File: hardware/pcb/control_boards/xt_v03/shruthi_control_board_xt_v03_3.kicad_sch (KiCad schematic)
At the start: 50 parts, among them IC2 74HC165N, IC3 74HC165N, IC8 74595N, IC9 74HC165N, SW1 Encoder

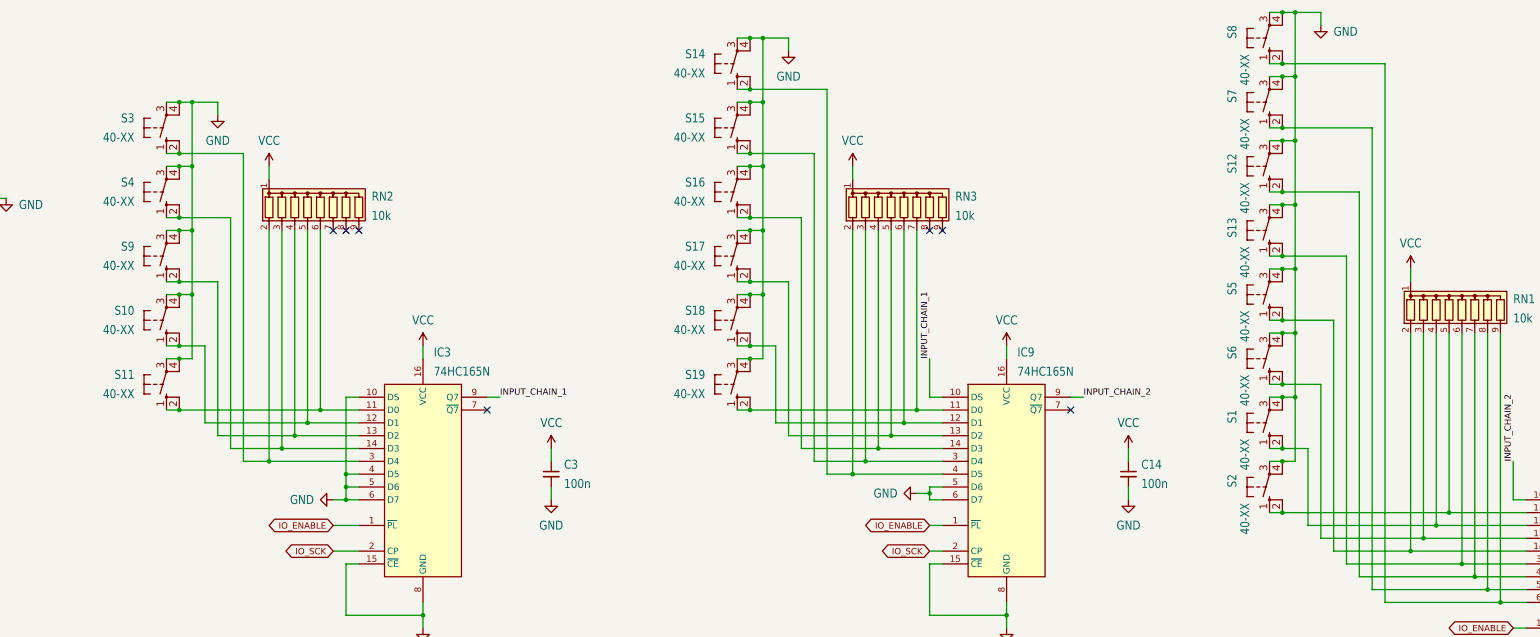
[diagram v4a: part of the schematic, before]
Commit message: update switches to use kicad symbols
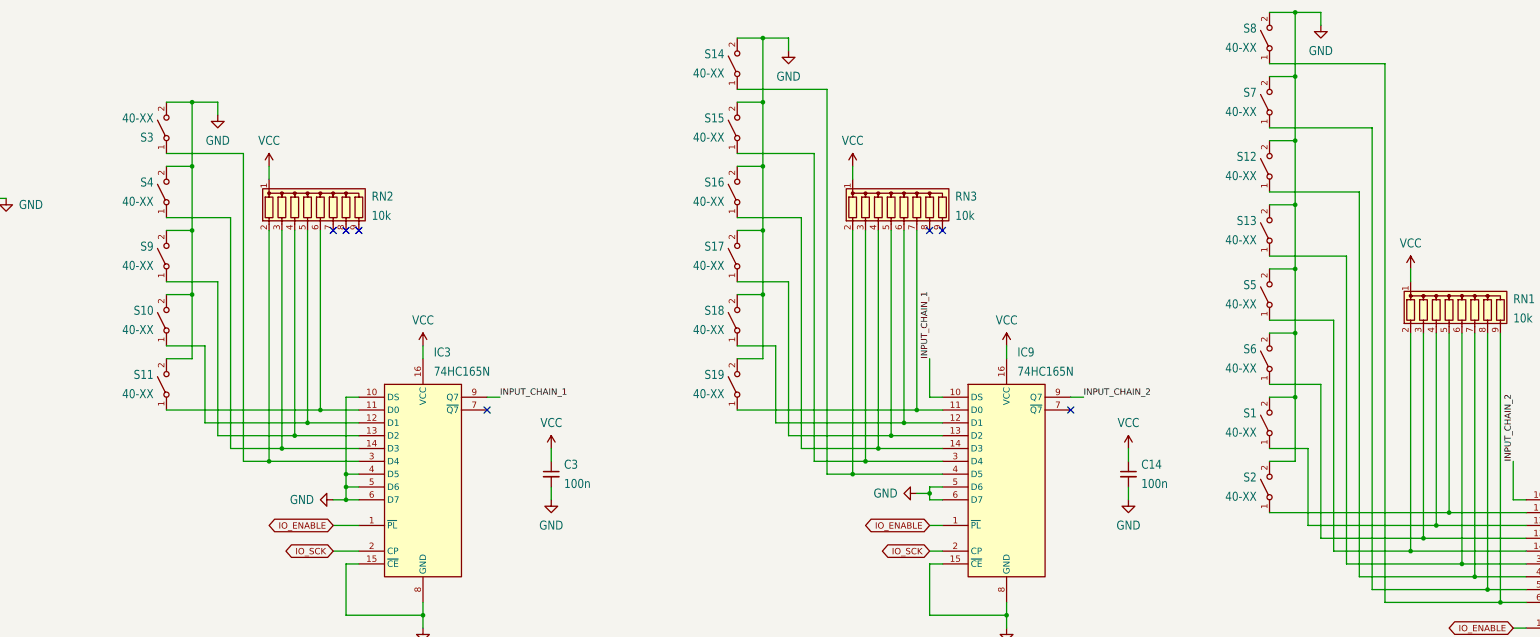
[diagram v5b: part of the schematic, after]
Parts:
- S1, S10, S11, S12, S13, S14, S15, S16, S17, S18, S19, S2, S3, S4, S5, S6, S7, S8, S9: symbol shruthi_control_board_xt_v03-eagle-import:40-XX -> Switch:SW_SPST
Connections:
- net GND: now also S1.2 (B), S10.2 (B), S11.2 (B), S12.2 (B), S13.2 (B), S14.2 (B), S15.2 (B), S16.2 (B), S17.2 (B), S18.2 (B), S19.2 (B), S2.2 (B), S3.2 (B), S4.2 (B), S5.2 (B), S6.2 (B), S7.2 (B), S8.2 (B), S9.2 (B); no longer S1.3 (P), S1.4 (P1), S10.3 (P), S10.4 (P1), S11.3 (P), S11.4 (P1), S12.3 (P), S12.4 (P1), S13.3 (P), S13.4 (P1), S14.3 (P), S14.4 (P1), S15.3 (P), S15.4 (P1), S16.3 (P), S16.4 (P1), S17.3 (P), S17.4 (P1), S18.3 (P), S18.4 (P1), S19.3 (P), S19.4 (P1), S2.3 (P), S2.4 (P1), S3.3 (P), S3.4 (P1), S4.3 (P), S4.4 (P1), S5.3 (P), S5.4 (P1), S6.3 (P), S6.4 (P1), S7.3 (P), S7.4 (P1), S8.3 (P), S8.4 (P1), S9.3 (P), S9.4 (P1)
- net at IC9.12 (D1), RN3.6 (R5), S18.1 (A): no longer S18.2 (S1)
- net at IC3.12 (D1), RN2.5 (R4), S10.1 (A): no longer S10.2 (S1)
- net at IC9.13 (D2), RN3.5 (R4), S17.1 (A): no longer S17.2 (S1)
- net at IC3.11 (D0), RN2.6 (R5), S11.1 (A): no longer S11.2 (S1)
- net at IC3.13 (D2), RN2.4 (R3), S9.1 (A): no longer S9.2 (S1)
- net at IC3.14 (D3), RN2.3 (R2), S4.1 (A): no longer S4.2 (S1)
- net at IC3.3 (D4), RN2.2 (R1), S3.1 (A): no longer S3.2 (S1)
- net at IC9.11 (D0), RN3.7 (R6), S19.1 (A): no longer S19.2 (S1)
- net at IC2.12 (D1), RN1.4 (R3), S1.1 (A): no longer S1.2 (S1)
- net at IC9.4 (D5), RN3.2 (R1), S14.1 (A): no longer S14.2 (S1)
- net at IC2.11 (D0), RN1.5 (R4), S2.1 (A): no longer S2.2 (S1)
- net at IC9.3 (D4), RN3.3 (R2), S15.1 (A): no longer S15.2 (S1)
- net at IC9.14 (D3), RN3.4 (R3), S16.1 (A): no longer S16.2 (S1)
- net at IC2.6 (D7), RN1.9 (R8), S8.1 (A): no longer S8.2 (S1)
- net at IC2.13 (D2), RN1.3 (R2), S6.1 (A): no longer S6.2 (S1)
- net at IC2.14 (D3), RN1.2 (R1), S5.1 (A): no longer S5.2 (S1)
- net at IC2.3 (D4), RN1.6 (R5), S13.1 (A): no longer S13.2 (S1)
- net at IC2.4 (D5), RN1.7 (R6), S12.1 (A): no longer S12.2 (S1)
- net at IC2.5 (D6), RN1.8 (R7), S7.1 (A): no longer S7.2 (S1)

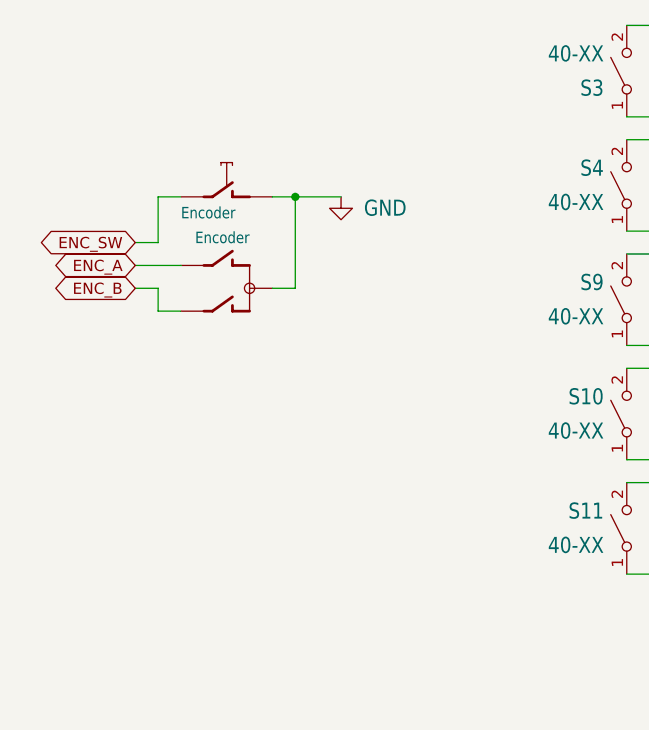
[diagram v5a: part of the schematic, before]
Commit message: update switches to use kicad symbols
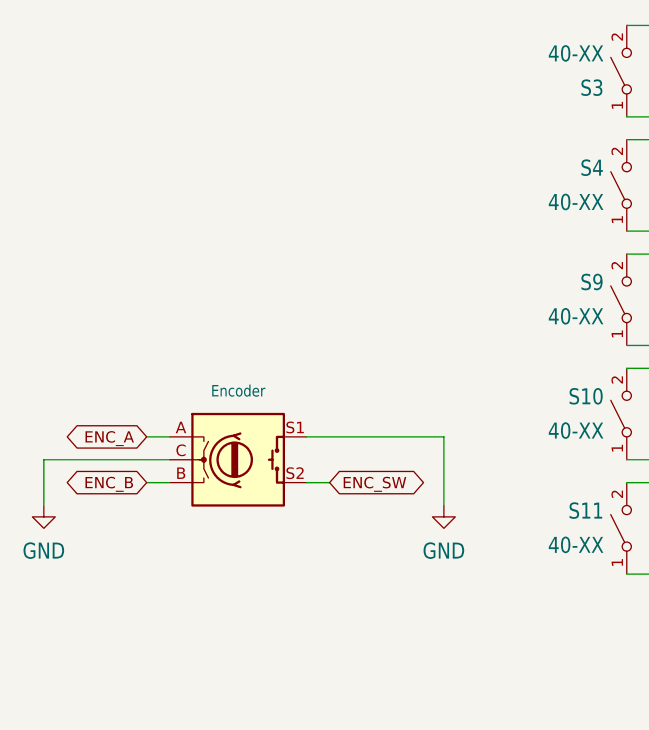
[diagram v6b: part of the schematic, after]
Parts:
- removed unit 2 of SW1
- SW1: symbol shruthi_control_board_xt_v03-eagle-import:EC12E_SW -> Device:RotaryEncoder_Switch
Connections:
- net ENC_A: now also SW1.A; no longer SW1.B
- net ENC_B: now also SW1.B; no longer SW1.A
- net ENC_SW: now also SW1.S2
- net GND: now also SW1.S1

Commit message: update 74HC165 footprints
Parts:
- IC2, IC3, IC9: footprint shruthi_control_board_xt_v03:DIL16 -> Package_DIP:DIP-16_W7.62mm_Socket_LongPads
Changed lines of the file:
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@@
 			)
 		)
-		(property "Footprint" "shruthi_control_board_xt_v03:DIL16"
+		(property "Footprint" "Package_DIP:DIP-16_W7.62mm_Socket_LongPads"
 			(at 139.7 127 0)
 			(effects
@@
 			)
 		)
-		(property "Footprint" "shruthi_control_board_xt_v03:DIL16"
+		(property "Footprint" "Package_DIP:DIP-16_W7.62mm_Socket_LongPads"
 			(at 255.27 127 0)
 			(effects
@@
 			)
 		)
-		(property "Footprint" "shruthi_control_board_xt_v03:DIL16"
+		(property "Footprint" "Package_DIP:DIP-16_W7.62mm_Socket_LongPads"
 			(at 370.84 147.32 0)
 			(effects

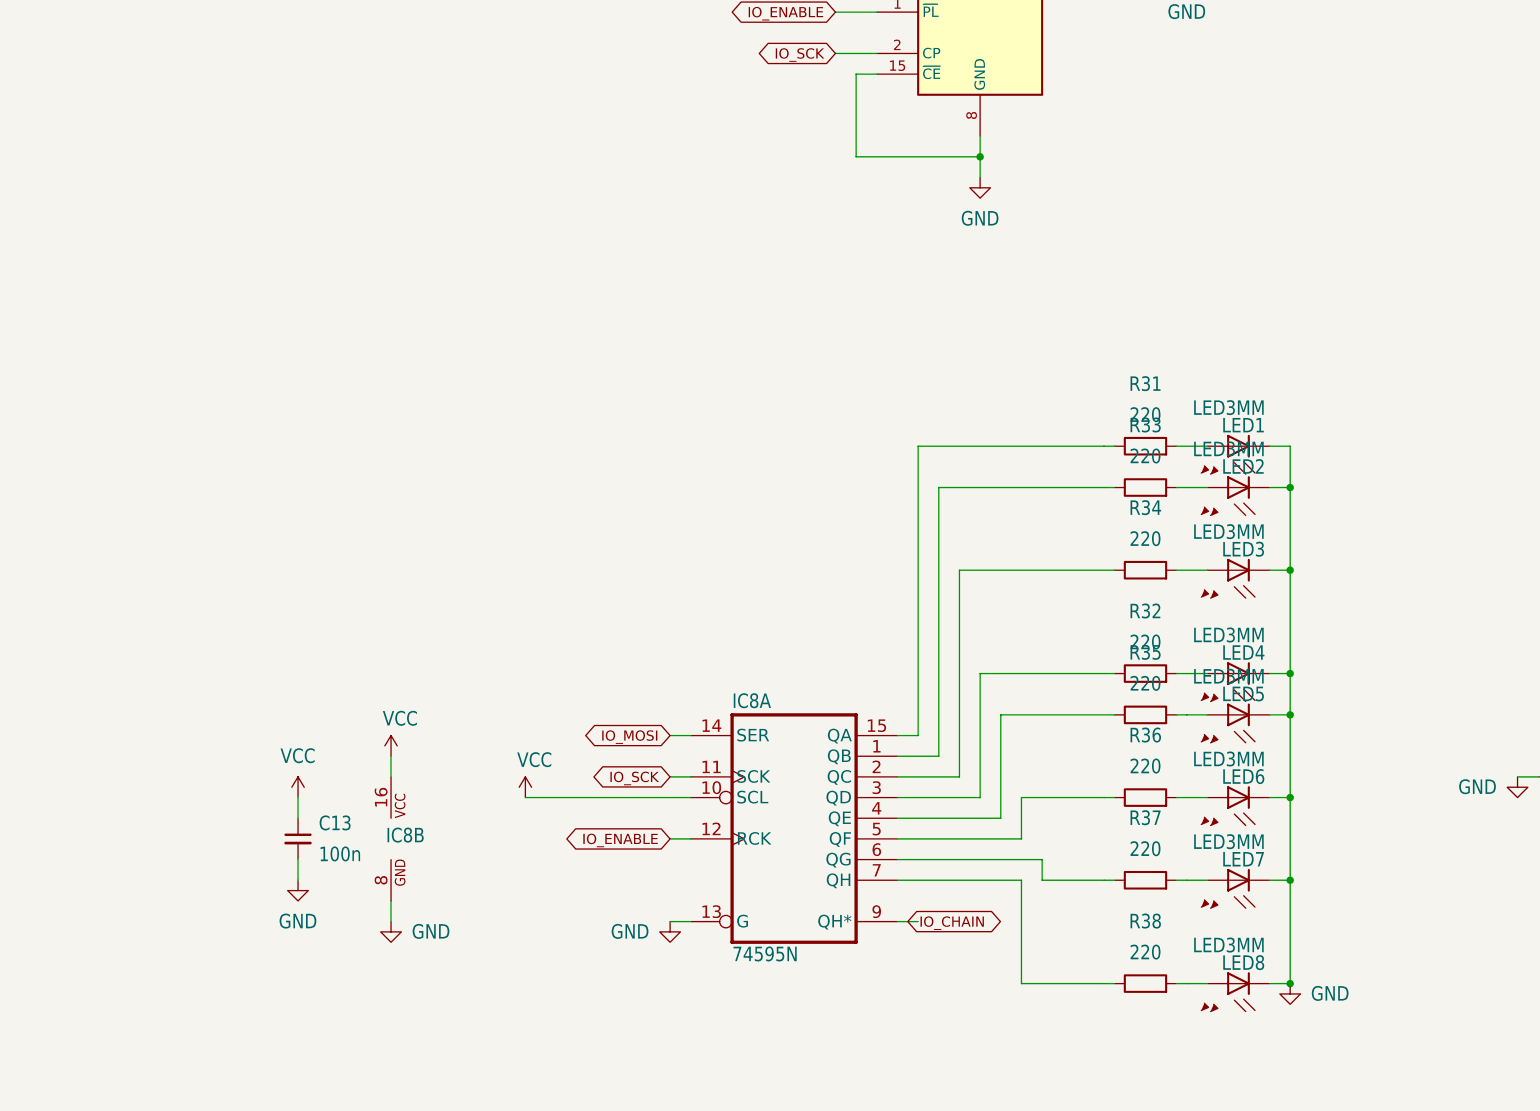
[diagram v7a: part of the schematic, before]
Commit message: update 74HC595 and LED symbols
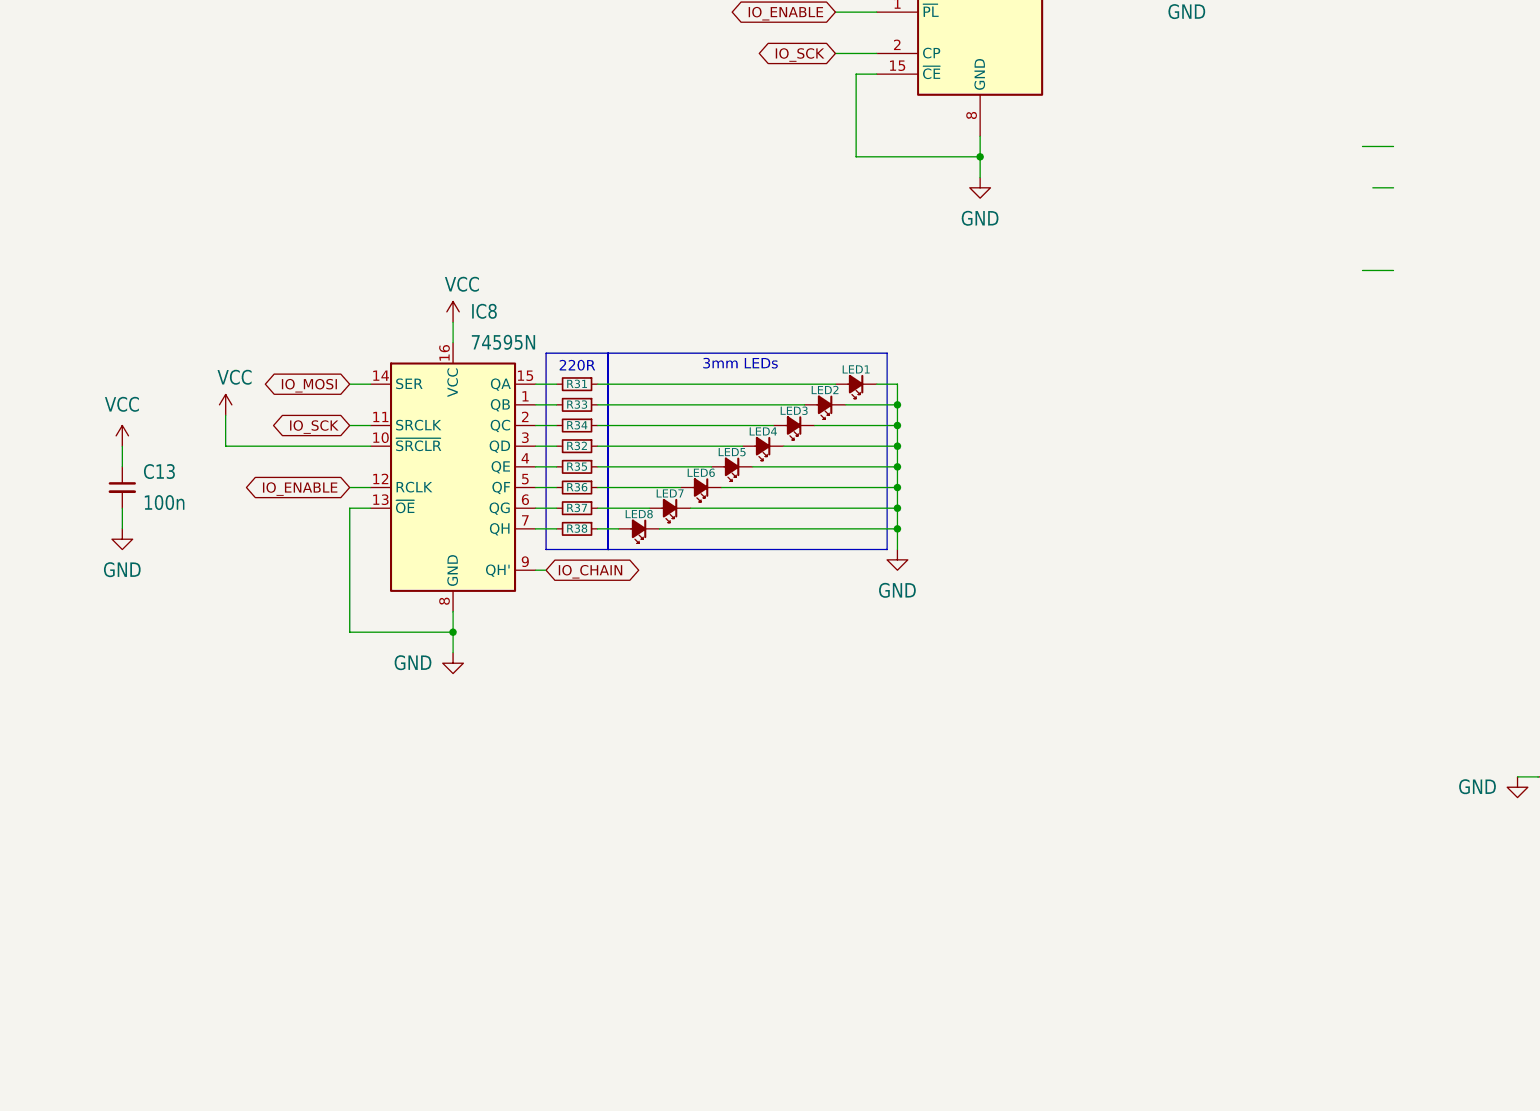
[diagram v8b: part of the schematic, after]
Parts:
- removed unit 2 of IC8
- IC8: symbol shruthi_control_board_xt_v03-eagle-import:74595N -> 74xx:74HC595
- LED1, LED2, LED3, LED4, LED5, LED6, LED7, LED8: symbol shruthi_control_board_xt_v03-eagle-import:LED3MM -> Device:LED_Small_Filled
- R31, R32, R33, R34, R35, R36, R37, R38: symbol Device:R -> Device:R_Small
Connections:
- net GND: now also IC8.8 (GND), LED1.1 (K), LED2.1 (K), LED3.1 (K), LED4.1 (K), LED5.1 (K), LED6.1 (K), LED7.1 (K), LED8.1 (K); no longer LED1.K (C), LED2.K (C), LED3.K (C), LED4.K (C), LED5.K (C), LED6.K (C), LED7.K (C), LED8.K (C)
- net VCC: now also IC8.16 (VCC)
- net at R35.1: now also LED5.2 (A); no longer IC8.4 (QE)
- net at R35.2: now also IC8.4 (QE); no longer LED5.A
- net at R33.2: now also IC8.1 (QB); no longer LED2.A
- net at R33.1: now also LED2.2 (A); no longer IC8.1 (QB)
- net at R37.2: now also IC8.6 (QG); no longer LED7.A
- net at R36.2: now also IC8.5 (QF); no longer LED6.A
- net at R37.1: now also LED7.2 (A); no longer IC8.6 (QG)
- net at R31.1: now also LED1.2 (A); no longer IC8.15 (QA)
- net at R31.2: now also IC8.15 (QA); no longer LED1.A
- net at R34.2: now also IC8.2 (QC); no longer LED3.A
- net at R36.1: now also LED6.2 (A); no longer IC8.5 (QF)
- net at R32.2: now also IC8.3 (QD); no longer LED4.A
- net at R34.1: now also LED3.2 (A); no longer IC8.2 (QC)
- net at R32.1: now also LED4.2 (A); no longer IC8.3 (QD)
- net at IC8.7 (QH): now also R38.2; no longer R38.1
- new net: LED8.2 (A), R38.1
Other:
- note added: "220R"
- note added: "3mm LEDs"
- moved on the sheet: C13, IC8, R31, R32, R33, R34, R35, R36, R37, R38
